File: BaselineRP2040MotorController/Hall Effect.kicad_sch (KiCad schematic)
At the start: 21 parts, among them J2 Encoder 1, U11 USBLC6-4SC6

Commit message: Drop some features.
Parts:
- J2: footprint RJ14 Footprint:RJ14_Connfly_DS1133-S6_Horizontal -> [EastMakes] Connectors:RJ14_Connfly_DS1133-S6_Horizontal
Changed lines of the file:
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@@
 			)
 		)
-		(property "Footprint" "RJ14 Footprint:RJ14_Connfly_DS1133-S6_Horizontal"
+		(property "Footprint" "[EastMakes] Connectors:RJ14_Connfly_DS1133-S6_Horizontal"
 			(at 52.07 71.12 0)
 			(effects

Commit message: Release for Review
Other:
- moved on the sheet: C39, C40, C41, C42, C43, C44, C45, C46, C47, C48, J2, JP1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

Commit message: Generate PDF
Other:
- title: (none) -> BLDC Starting Point
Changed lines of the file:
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@@
 	(generator_version "8.0")
 	(paper "A5")
+	(title_block
+		(title "BLDC Starting Point")
+		(comment 1 "Florian, Josh and EMF Group Release")
+	)
 	(junction
 		(at 71.12 39.37)

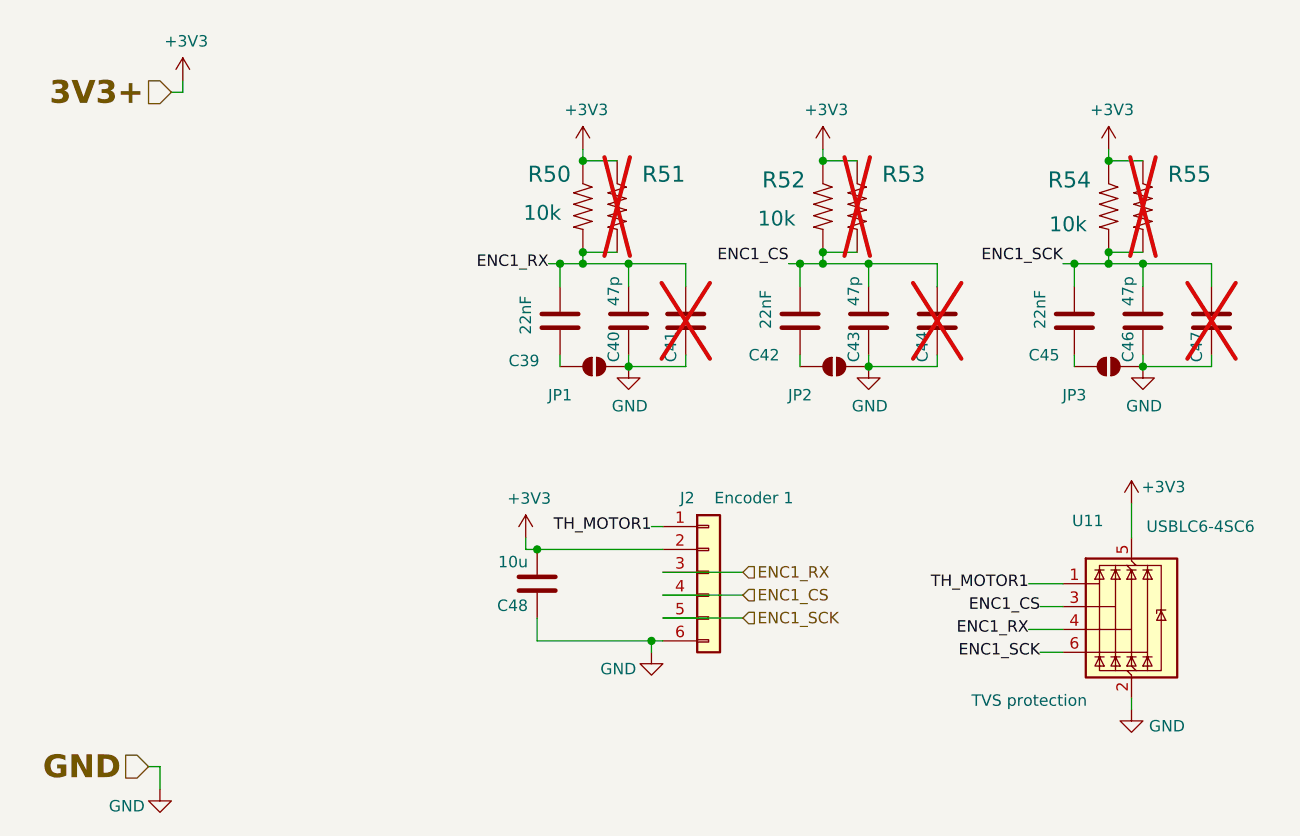
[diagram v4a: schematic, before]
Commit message: Make a cut down board.
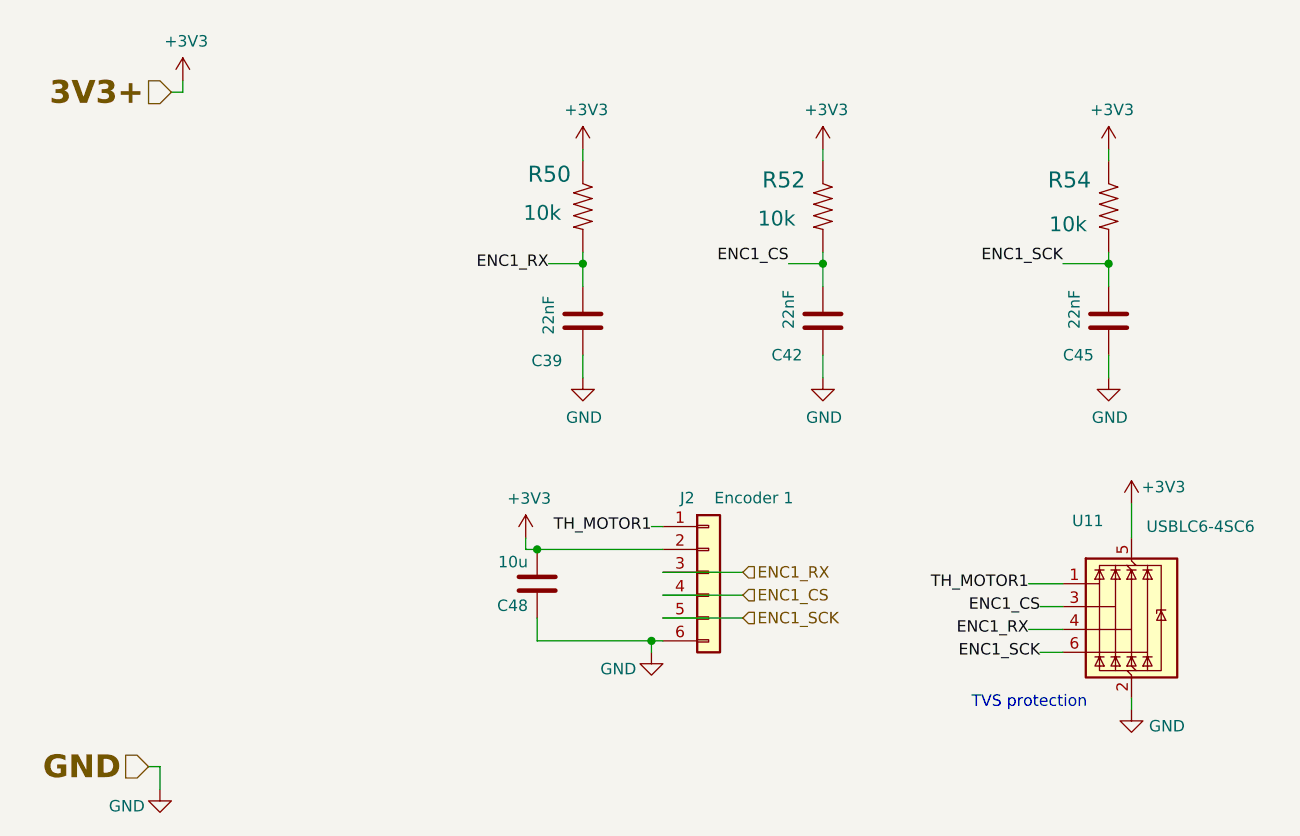
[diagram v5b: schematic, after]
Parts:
- removed C40, C43, C46: 47p, Capacitor_SMD:C_0603_1608Metric, symbol Device:C
- removed C41, C44, C47: ~, Capacitor_SMD:C_0805_2012Metric, symbol Device:C
- removed JP1, JP2, JP3: SolderJumper_2_Open, Jumper:SolderJumper-2_P1.3mm_Open_RoundedPad1.0x1.5mm, symbol Jumper:SolderJumper_2_Open
- removed R51, R53, R55: ~, Resistor_SMD:R_0805_2012Metric, symbol MotorController:TAYLOR_RESISTOR
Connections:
- net GND: now also C39.1, C42.2, C45.2
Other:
- moved on the sheet: C39, C42, C45
